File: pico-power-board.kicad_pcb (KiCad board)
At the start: 2 copper layers, 120 x 70 mm, 79 parts, among them J1 Conn_02x10_Counter_Clockwise, J10 Conn_01x20_Female, J2 Conn_02x10_Counter_Clockwise, J3 Conn_02x10_Counter_Clockwise, J4 Conn_02x10_Counter_Clockwise, J5 Conn_02x10_Counter_Clockwise, J6 Conn_02x10_Counter_Clockwise, J7 DC-042C-Z-2.5, J8 Conn_01x06_Male, J9 Conn_01x20_Female, U1 INA219AxD, U2 TMP112AIDRLR, U3 K7803-500R3

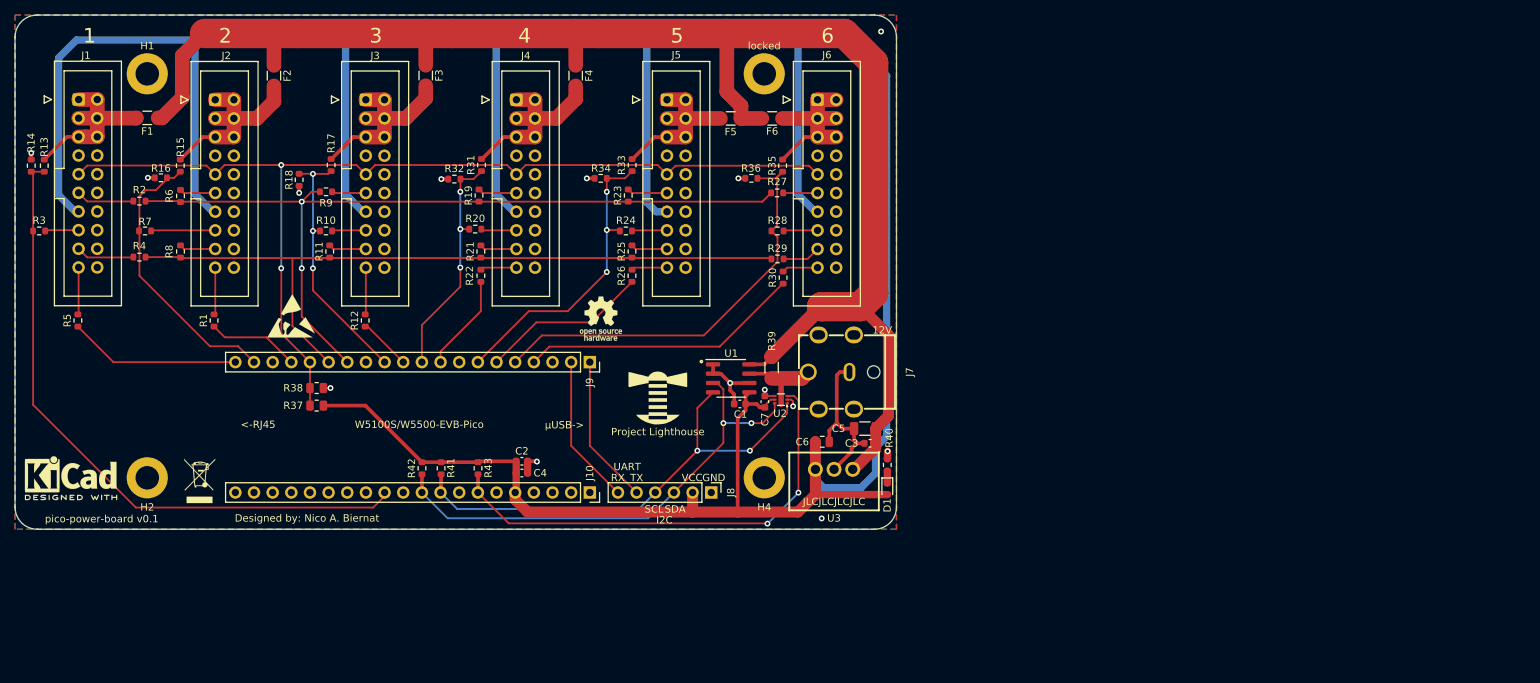
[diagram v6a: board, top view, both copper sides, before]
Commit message: Add tri-state buffers to each connectors MISO line in order to Thevenin-terminate them separately and add decoupling capacitors to the termination, change LED and series resistor, change I2C pull-ups, add CS pull-ups, add MISO pull-down (after buffers)
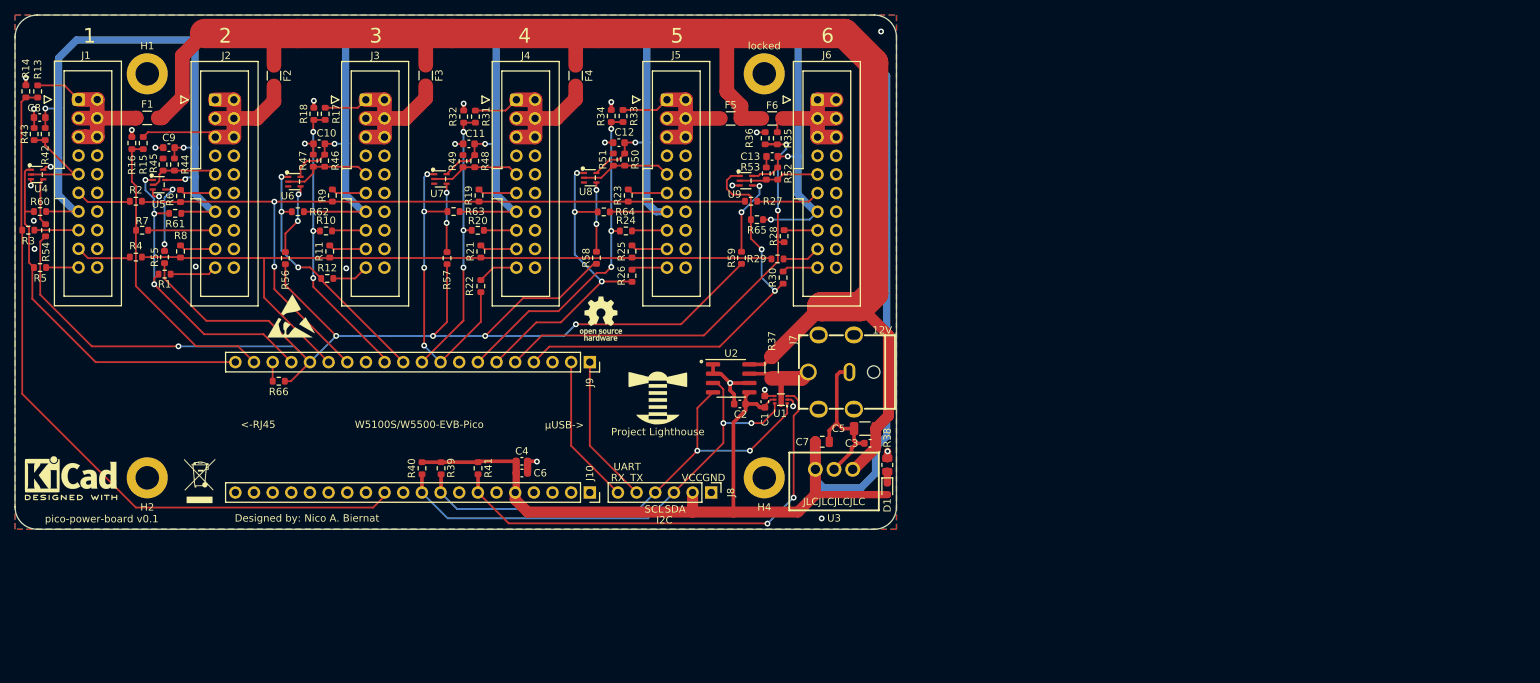
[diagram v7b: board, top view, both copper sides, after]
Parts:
- removed the R37 at (131.1, 128.2)
- removed the R38 at (131.1, 125.8)
- added C10: 100nF, Capacitor_SMD:C_0603_1608Metric, F.Cu at (131.4, 92.5)
- added C11: 100nF, Capacitor_SMD:C_0603_1608Metric, F.Cu at (151.8, 92.5)
- added C12: 100nF, Capacitor_SMD:C_0603_1608Metric, F.Cu at (172.2, 92.4)
- added C13: 100nF, Capacitor_SMD:C_0603_1608Metric, F.Cu at (193.1, 94.2)
- added C8: 100nF, Capacitor_SMD:C_0603_1608Metric, F.Cu at (93.3, 89.0)
- added C9: 100nF, Capacitor_SMD:C_0603_1608Metric, F.Cu at (111.0, 93.0)
- added R42: 200, Resistor_SMD:R_0603_1608Metric, F.Cu at (94.1, 91.2)
- added R43: 200, Resistor_SMD:R_0603_1608Metric, F.Cu at (92.6, 91.2)
- added R44: 200, Resistor_SMD:R_0603_1608Metric, F.Cu at (111.7, 95.3)
- added R45: 200, Resistor_SMD:R_0603_1608Metric, F.Cu at (110.2, 95.3)
- added R46: 200, Resistor_SMD:R_0603_1608Metric, F.Cu at (132.2, 94.8)
- added R47: 200, Resistor_SMD:R_0603_1608Metric, F.Cu at (130.6, 94.8)
- added R48: 200, Resistor_SMD:R_0603_1608Metric, F.Cu at (152.6, 94.9)
- added R49: 200, Resistor_SMD:R_0603_1608Metric, F.Cu at (151.0, 94.9)
- added R50: 200, Resistor_SMD:R_0603_1608Metric, F.Cu at (173.0, 94.7)
- added R51: 200, Resistor_SMD:R_0603_1608Metric, F.Cu at (171.4, 94.7)
- added R52: 200, Resistor_SMD:R_0603_1608Metric, F.Cu at (193.8, 96.6)
- added R53: 200, Resistor_SMD:R_0603_1608Metric, F.Cu at (192.3, 96.6)
- added R54: 100, Resistor_SMD:R_0603_1608Metric, F.Cu at (94.2, 104.3)
- added R55: 100, Resistor_SMD:R_0603_1608Metric, F.Cu at (110.3, 108.0)
- added R56: 100, Resistor_SMD:R_0603_1608Metric, F.Cu at (126.8, 108.1)
- added R57: 100, Resistor_SMD:R_0603_1608Metric, F.Cu at (148.8, 108.1)
- added R58: 100, Resistor_SMD:R_0603_1608Metric, F.Cu at (169.2, 108.0)
- added R59: 100, Resistor_SMD:R_0603_1608Metric, F.Cu at (188.9, 108.0)
- added R60: 10k, Resistor_SMD:R_0603_1608Metric, F.Cu at (93.4, 101.8)
- added R61: 10k, Resistor_SMD:R_0603_1608Metric, F.Cu at (111.8, 102.0)
- added R62: 10k, Resistor_SMD:R_0603_1608Metric, F.Cu at (128.5, 101.8)
- added R63: 10k, Resistor_SMD:R_0603_1608Metric, F.Cu at (149.7, 101.8)
- added R64: 10k, Resistor_SMD:R_0603_1608Metric, F.Cu at (170.2, 101.8)
- added R65: 10k, Resistor_SMD:R_0603_1608Metric, F.Cu at (191.0, 102.8)
- added R66: 10k, Resistor_SMD:R_0603_1608Metric, F.Cu at (125.9, 124.8)
- added U4: 74LVC1G125GW,125, Lighthouse:SOT-353_L2.1-W1.3-P0.65-LS2.3-BR, F.Cu at (93.0, 96.7)
- added U5: 74LVC1G125GW,125, Lighthouse:SOT-353_L2.1-W1.3-P0.65-LS2.3-BR, F.Cu at (109.6, 98.1)
- added U6: 74LVC1G125GW,125, Lighthouse:SOT-353_L2.1-W1.3-P0.65-LS2.3-BR, F.Cu at (128.0, 97.7)
- added U7: 74LVC1G125GW,125, Lighthouse:SOT-353_L2.1-W1.3-P0.65-LS2.3-BR, F.Cu at (147.9, 97.3)
- added U8: 74LVC1G125GW,125, Lighthouse:SOT-353_L2.1-W1.3-P0.65-LS2.3-BR, F.Cu at (168.3, 97.2)
- added U9: 74LVC1G125GW,125, Lighthouse:SOT-353_L2.1-W1.3-P0.65-LS2.3-BR, F.Cu at (189.5, 97.5)
- R38: renamed from R40; value 68 -> 470; footprint Resistor_SMD:R_0603_1608Metric -> Resistor_SMD:R_0805_2012Metric
- R39: renamed from R41; value 3.3k -> 4.7k
- R40: renamed from R42; value 3.3k -> 4.7k
- R41: renamed from R43; value 3.3k -> 4.7k
- moved R13 10.1 mm to (93.1, 85.4)
- moved R14 10.1 mm to (91.5, 85.4)
- moved R1 9.23 mm to (110.4, 110.3), turned to 0 degrees
- moved R18 9.20 mm to (130.7, 88.5), turned to -90 degrees
- moved R5 8.86 mm to (93.4, 109.4), turned to 0 degrees
- moved R34 8.61 mm to (171.2, 88.7), turned to -90 degrees
- moved R32 8.60 mm to (151.1, 88.8), turned to -90 degrees
- moved R12 7.71 mm to (132.5, 110.9), turned to 0 degrees
- moved R17 7.02 mm to (132.2, 88.4)
- moved R33 6.80 mm to (172.8, 88.7)
- moved R31 6.65 mm to (152.7, 88.8)
- moved R16 6.17 mm to (105.9, 92.4), turned to -90 degrees
- moved R15 5.91 mm to (107.5, 92.4)
- moved R36 5.77 mm to (192.1, 91.8), turned to -90 degrees
- moved R35 3.79 mm to (193.8, 91.8)
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- renumbered C7 to C1, C1 to C2, C2 to C4, C4 to C6, C6 to C7, G*** to G_LH, R39 to R37, REF** to REF_ESD, REF** to REF_KiCad, REF** to REF_OSH, REF** to REF_WEEE, U2 to U1, U1 to U2
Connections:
- J1 pad 15: MISO -> MISO_1
- J2 pad 15: MISO -> MISO_2
- J3 pad 15: MISO -> MISO_3
- J4 pad 15: MISO -> MISO_4
- J5 pad 15: MISO -> MISO_5
- J6 pad 15: MISO -> MISO_6
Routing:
- net +3V3: track 446.7 -> 523.2 mm, vias 0 -> 9
- net MISO: track 140.1 -> 186.6 mm, vias 2 -> 5
- net CS2: track 12.5 -> 42.4 mm, vias 0 -> 3
- net CS4: track 13.2 -> 42.6 mm, vias 0 -> 4
- net CS3: track 7.19 -> 35.4 mm, vias 0 -> 3
- net CS1: track 23.4 -> 51.3 mm
- net CS6: track 38.4 -> 59.4 mm, vias 0 -> 2
- net CS5: track 23.0 -> 43.5 mm, vias 0 -> 3
- net GND: track 46.5 -> 62.1 mm, vias 14 -> 25
- net MISO_1: track 0.00 -> 14.9 mm
- net MISO_5: track 0.00 -> 12.5 mm
- net MISO_3: track 0.00 -> 12.4 mm
- net MISO_4: track 0.00 -> 12.3 mm
- net Net-(U9-Y): track 0.00 -> 11.0 mm, vias 0 -> 2
- net MISO_6: track 0.00 -> 11.0 mm
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
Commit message: Revision v0.1
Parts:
- R13, R15, R17, R31, R33, R35: value 30k -> 27k
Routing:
- net GND: track 62.1 -> 63.1 mm, vias 25 -> 26
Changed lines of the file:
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@@
     (tags "resistor")
     (property "JLC" "0603")
-    (property "LCSC" "C22984")
+    (property "LCSC" "C308131")
     (property "Sheetfile" "pico-power-board.kicad_sch")
     (property "Sheetname" "")
@@
         (effects (font (size 1 1) (thickness 0.15)))
     )
-    (fp_text value "30k" (at 0 1.43 90) (layer "F.Fab")
+    (fp_text value "27k" (at 0 1.43 90) (layer "F.Fab")
         (effects (font (size 1 1) (thickness 0.15)))
     )
@@
     (tags "resistor")
     (property "JLC" "0603")
-    (property "LCSC" "C22984")
+    (property "LCSC" "C308131")
     (property "Sheetfile" "pico-power-board.kicad_sch")
     (property "Sheetname" "")
@@
         (effects (font (size 1 1) (thickness 0.15)))
     )
-    (fp_text value "30k" (at 0 1.43 90) (layer "F.Fab")
+    (fp_text value "27k" (at 0 1.43 90) (layer "F.Fab")
         (effects (font (size 1 1) (thickness 0.15)))
     )
@@
     (tags "resistor")
     (property "JLC" "0603")
-    (property "LCSC" "C22984")
+    (property "LCSC" "C308131")
     (property "Sheetfile" "pico-power-board.kicad_sch")
     (property "Sheetname" "")
@@
         (effects (font (size 1 1) (thickness 0.15)))
     )
-    (fp_text value "30k" (at 0 1.43 90) (layer "F.Fab")
+    (fp_text value "27k" (at 0 1.43 90) (layer "F.Fab")
         (effects (font (size 1 1) (thickness 0.15)))
     )
@@
     (fp_line (start 1 0.625) (end -1 0.625)
       (stroke (width 0.1) (type solid)) (layer "F.Fab"))
-    (pad "1" smd roundrect (at -0.9125 0 270) (size 1.025 1.4) (layers "F.Cu" "F.Paste" "F.Mask") (roundrect_rratio 0.243902)
+    (pad "1" smd roundrect (at -0.9125 0 270) (size 1.025 1.4) (layers "F.Cu" "F.Paste" "F.Mask") (roundrect_rratio 0.243902439)
       (net 10 "GND") (pintype "passive"))
-    (pad "2" smd roundrect (at 0.9125 0 270) (size 1.025 1.4) (layers "F.Cu" "F.Paste" "F.Mask") (roundrect_rratio 0.243902)
+    (pad "2" smd roundrect (at 0.9125 0 270) (size 1.025 1.4) (layers "F.Cu" "F.Paste" "F.Mask") (roundrect_rratio 0.243902439)
       (net 7 "Net-(D1-K)") (pintype "passive"))
     (model "${KICAD6_3DMODEL_DIR}/Resistor_SMD.3dshapes/R_0805_2012Metric.wrl"
@@
     (property "ki_keywords" "R res resistor")
     (attr smd)
-    (fp_text reference "R14" (at -3.111 0 90) (layer "F.SilkS")
+    (fp_text reference "R14" (at -3.64 0 90) (layer "F.SilkS")
         (effects (font (size 1 1) (thickness 0.15)))
     )
@@
     (tags "resistor")
     (property "JLC" "0603")
-    (property "LCSC" "C22984")
+    (property "LCSC" "C308131")
     (property "Sheetfile" "pico-power-board.kicad_sch")
     (property "Sheetname" "")
@@
         (effects (font (size 1 1) (thickness 0.15)))
     )
-    (fp_text value "30k" (at 0 1.43 90) (layer "F.Fab")
+    (fp_text value "27k" (at 0 1.43 90) (layer "F.Fab")
         (effects (font (size 1 1) (thickness 0.15)))
     )
@@
     (tags "resistor")
     (property "JLC" "0603")
-    (property "LCSC" "C22984")
+    (property "LCSC" "C308131")
     (property "Sheetfile" "pico-power-board.kicad_sch")
     (property "Sheetname" "")
@@
         (effects (font (size 1 1) (thickness 0.15)))
     )
-    (fp_text value "30k" (at 0 1.43 90) (layer "F.Fab")
+    (fp_text value "27k" (at 0 1.43 90) (layer "F.Fab")
         (effects (font (size 1 1) (thickness 0.15)))
     )
@@
     (property "ki_keywords" "cap capacitor")
     (attr smd)
-    (fp_text reference "C8" (at 0.75 1.3) (layer "F.SilkS")
+    (fp_text reference "C8" (at 2.05 0 90) (layer "F.SilkS")
         (effects (font (size 1 1) (thickness 0.15)))
     )
@@
     (tags "resistor")
     (property "JLC" "0603")
-    (property "LCSC" "C22984")
+    (property "LCSC" "C308131")
     (property "Sheetfile" "pico-power-board.kicad_sch")
     (property "Sheetname" "")
@@
         (effects (font (size 1 1) (thickness 0.15)))
     )
-    (fp_text value "30k" (at 0 1.43 90) (layer "F.Fab")
+    (fp_text value "27k" (at 0 1.43 90) (layer "F.Fab")
         (effects (font (size 1 1) (thickness 0.15)))
     )
@@
     (property "ki_keywords" "cap capacitor")
     (attr smd)
-    (fp_text reference "C13" (at 2.975 0) (layer "F.SilkS")
+    (fp_text reference "C13" (at 3.825 0) (layer "F.SilkS")
         (effects (font (size 1 1) (thickness 0.15)))
     )
@@
     (property "ki_keywords" "R res resistor")
     (attr smd)
-    (fp_text reference "R43" (at 0 -1.3 90) (layer "F.SilkS")
+    (fp_text reference "R43" (at -0.6 -1.3 90) (layer "F.SilkS")
         (effects (font (size 1 1) (thickness 0.15)))
     )
@@
   (segment (start 185.025 123.825) (end 185.025 122.555) (width 0.5) (layer "F.Cu") (net 10))
   (segment (start 204.57 133.3) (end 204.56 133.3) (width 0.5) (layer "F.Cu") (net 10))
+  (segment (start 191.25 94.25) (end 192.3 94.25) (width 0.25) (layer "F.Cu") (net 10))
   (segment (start 130.6 92.5) (end 130.625 92.525) (width 0.25) (layer "F.Cu") (net 10))
   (segment (start 204.225 131.3) (end 204.225 132.955) (width 0.5) (layer "F.Cu") (net 10))
@@
   (via (at 190.975 90.975) (size 0.8) (drill 0.4) (layers "F.Cu" "B.Cu") (free) (net 10))
   (via (at 208.788 134.39) (size 0.8) (drill 0.4) (layers "F.Cu" "B.Cu") (free) (net 10))
+  (via (at 191.25 94.25) (size 0.8) (drill 0.4) (layers "F.Cu" "B.Cu") (free) (net 10))
   (via (at 199.82 143.53) (size 0.8) (drill 0.4) (layers "F.Cu" "B.Cu") (free) (net 10))
   (via (at 149.9 92.55) (size 0.8) (drill 0.4) (layers "F.Cu" "B.Cu") (free) (net 10))
